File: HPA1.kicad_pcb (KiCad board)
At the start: 2 copper layers, 98.4 x 73 mm, 96 parts, among them J1 Power, J2 Input, J3 Output, J4 Mute, J5 Conn_01x01_Male, K1 G6H-2, Q1 BC560C, Q10 BC549C, Q11 BC549C, Q12 TTA004B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

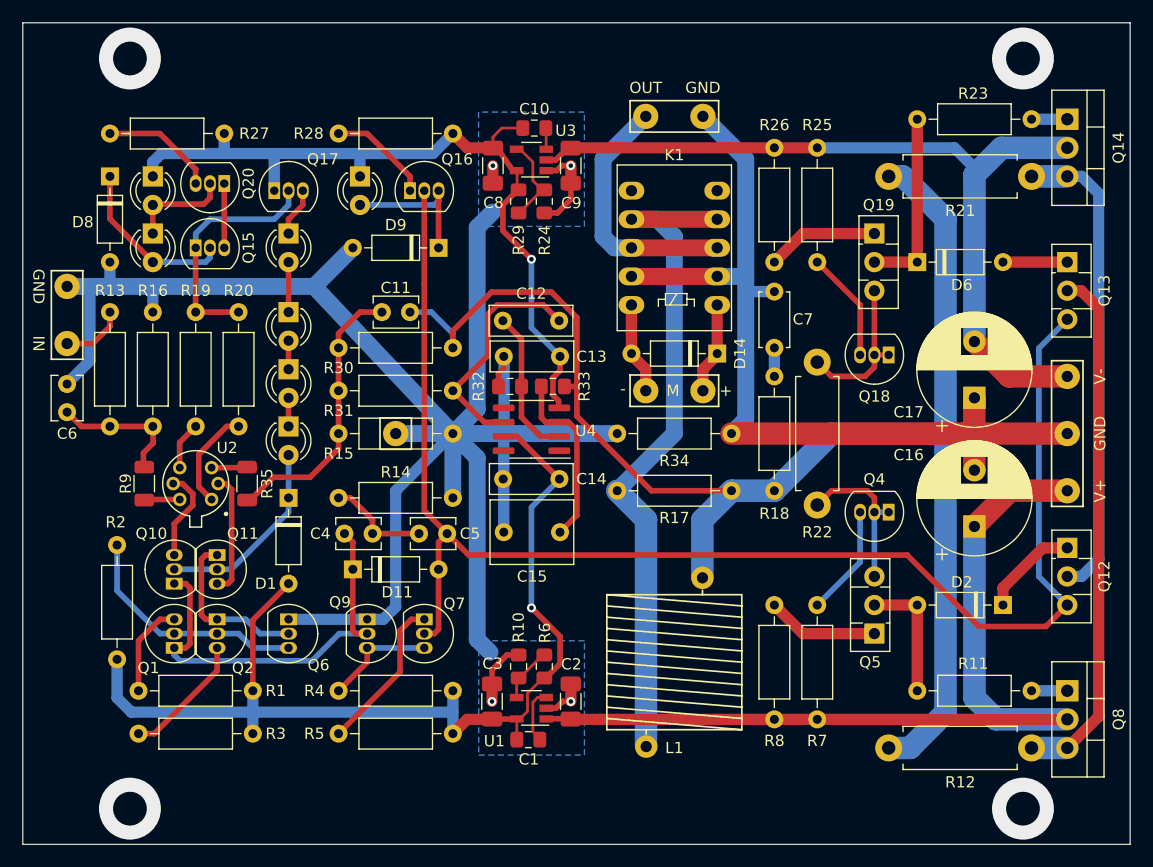
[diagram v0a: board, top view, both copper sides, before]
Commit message: Converted to KiCad 9.0.
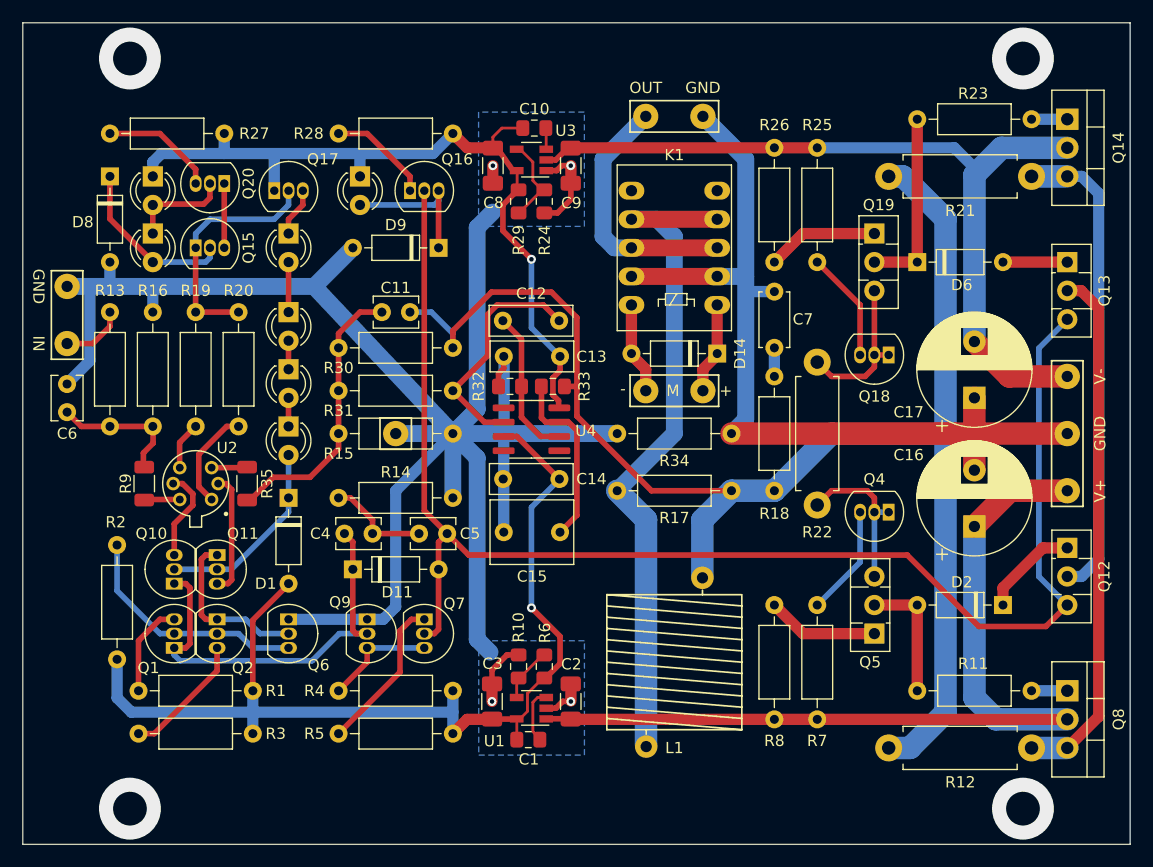
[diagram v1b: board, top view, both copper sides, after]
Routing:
- net Net-(K1-Pad4): track 62.1 -> 60.4 mm

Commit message: Created local symbol and footprint libraries. Updated schematic and PCB. Fixed all rule check errors.
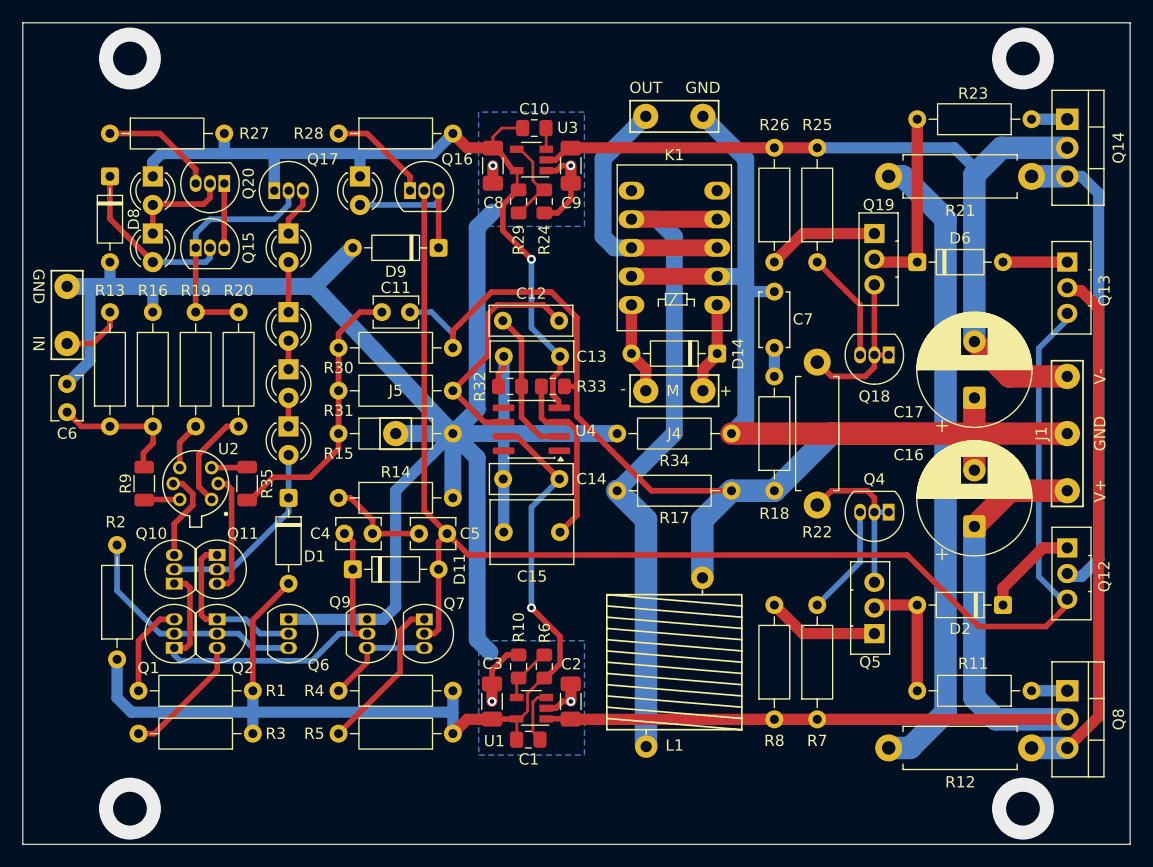
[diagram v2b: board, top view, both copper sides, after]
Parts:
- C1, C10: footprint Capacitor_SMD:C_0805_2012Metric_Pad1.15x1.40mm_HandSolder -> Capacitor_SMD:C_0805_2012Metric_Pad1.18x1.45mm_HandSolder
- D1, D11, D14, D2, D6, D8, D9: footprint Diode_THT:D_DO-35_SOD27_P7.62mm_Horizontal -> HPA1-footprints:D_DO-35_SOD27_P7.62mm_Horizontal
- J1: footprint HP_Footprints:3-pad-wire-connector-22-ga -> HPA1-footprints:3-pad-wire-connector-22-ga
- J2, J3, J4: footprint HP_Footprints:2-pad-wire-connector-22-ga -> HPA1-footprints:2-pad-wire-connector-22-ga
- J5: footprint HP_Footprints:1-pad-wire-connector-22-ga -> HPA1-footprints:1-pad-wire-connector-22-ga
- L1: footprint HP_Footprints:HPA-Output-Coil -> HPA1-footprints:HPA-Output-Coil
- R10, R24, R29, R32, R33, R6: footprint Resistor_SMD:R_0805_2012Metric_Pad1.15x1.40mm_HandSolder -> HPA1-footprints:R_0805_2012Metric_Pad1.15x1.40mm_HandSolder
- U1, U3: footprint Package_TO_SOT_SMD:TSOT-23-5 -> HPA1-footprints:TSOT-23-5
- U2: footprint HP_Footprints:TO-71-6 -> HPA1-footprints:TO-71-6
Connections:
- K1 pad 5: Net-(K1-Pad5) -> unconnected-(K1-NC-Pad5)
- K1 pad 6: Net-(K1-Pad6) -> unconnected-(K1-NC-Pad6)
- U4 pad 1: Net-(U4-Pad1) -> unconnected-(U4-N-Pad1)
- U4 pad 5: Net-(U4-Pad5) -> unconnected-(U4-N-Pad5)
- U4 pad 8: (no net) -> unconnected-(U4-Pad8)
